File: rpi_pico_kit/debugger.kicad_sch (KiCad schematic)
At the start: 34 parts, among them J3 USB_B_Mini, U2 RP2040, U3 NCP1117-3.3_SOT223, U4 W25Q128JVS, Y1 12MHz

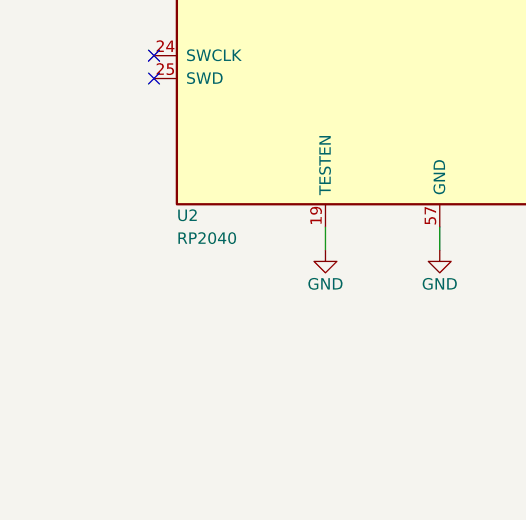
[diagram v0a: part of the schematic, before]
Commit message: changed transistors to unused gates of 7414
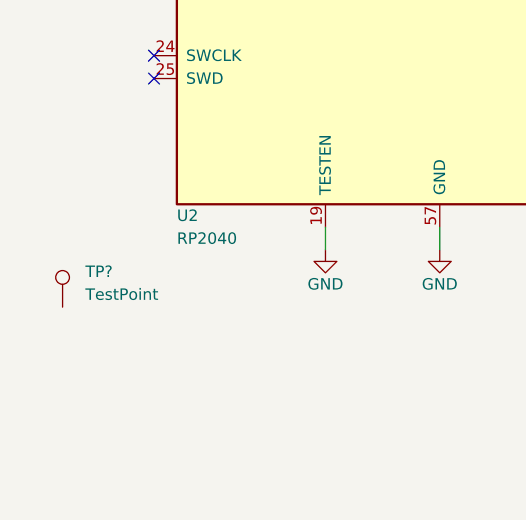
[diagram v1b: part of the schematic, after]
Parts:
- added TP?: TestPoint, symbol Connector:TestPoint
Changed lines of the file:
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@@
     (effects (font (size 1.27 1.27)) (justify left))
+  )
+  (symbol (lib_id "Connector:TestPoint") (at 27.94 168.91 0) (unit 1)
+    (in_bom yes) (on_board yes) (fields_autoplaced)
+    (property "Reference" "TP?" (id 0) (at 30.48 164.973 0)
+      (effects (font (size 1.27 1.27)) (justify left))
+    )
+    (property "Value" "TestPoint" (id 1) (at 30.48 167.513 0)
+      (effects (font (size 1.27 1.27)) (justify left))
+    )
+    (property "Footprint" "" (id 2) (at 33.02 168.91 0)
+      (effects (font (size 1.27 1.27)) hide)
+    )
+    (property "Datasheet" "~" (id 3) (at 33.02 168.91 0)
+      (effects (font (size 1.27 1.27)) hide)
+    )
+    (pin "1")
   )
   (symbol (lib_id "MCU_RaspberryPi_RP2040:RP2040") (at 69.85 109.22 0) (unit 1)

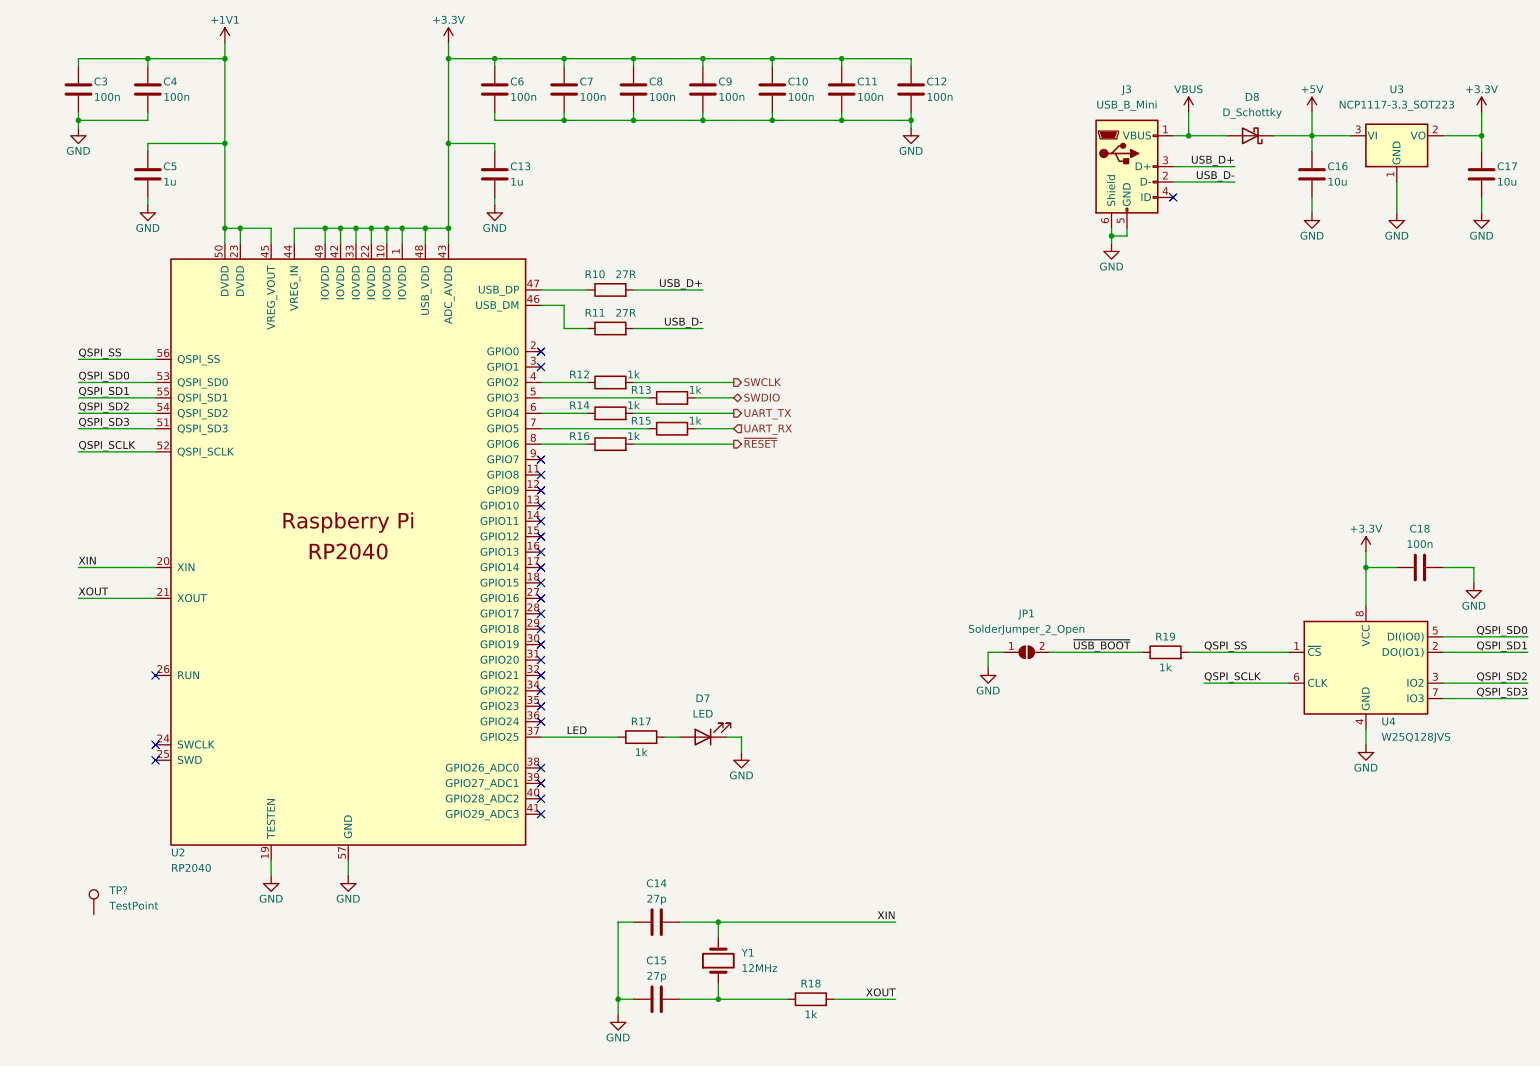
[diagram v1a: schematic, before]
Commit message: added test pads for uart and swd of debugger
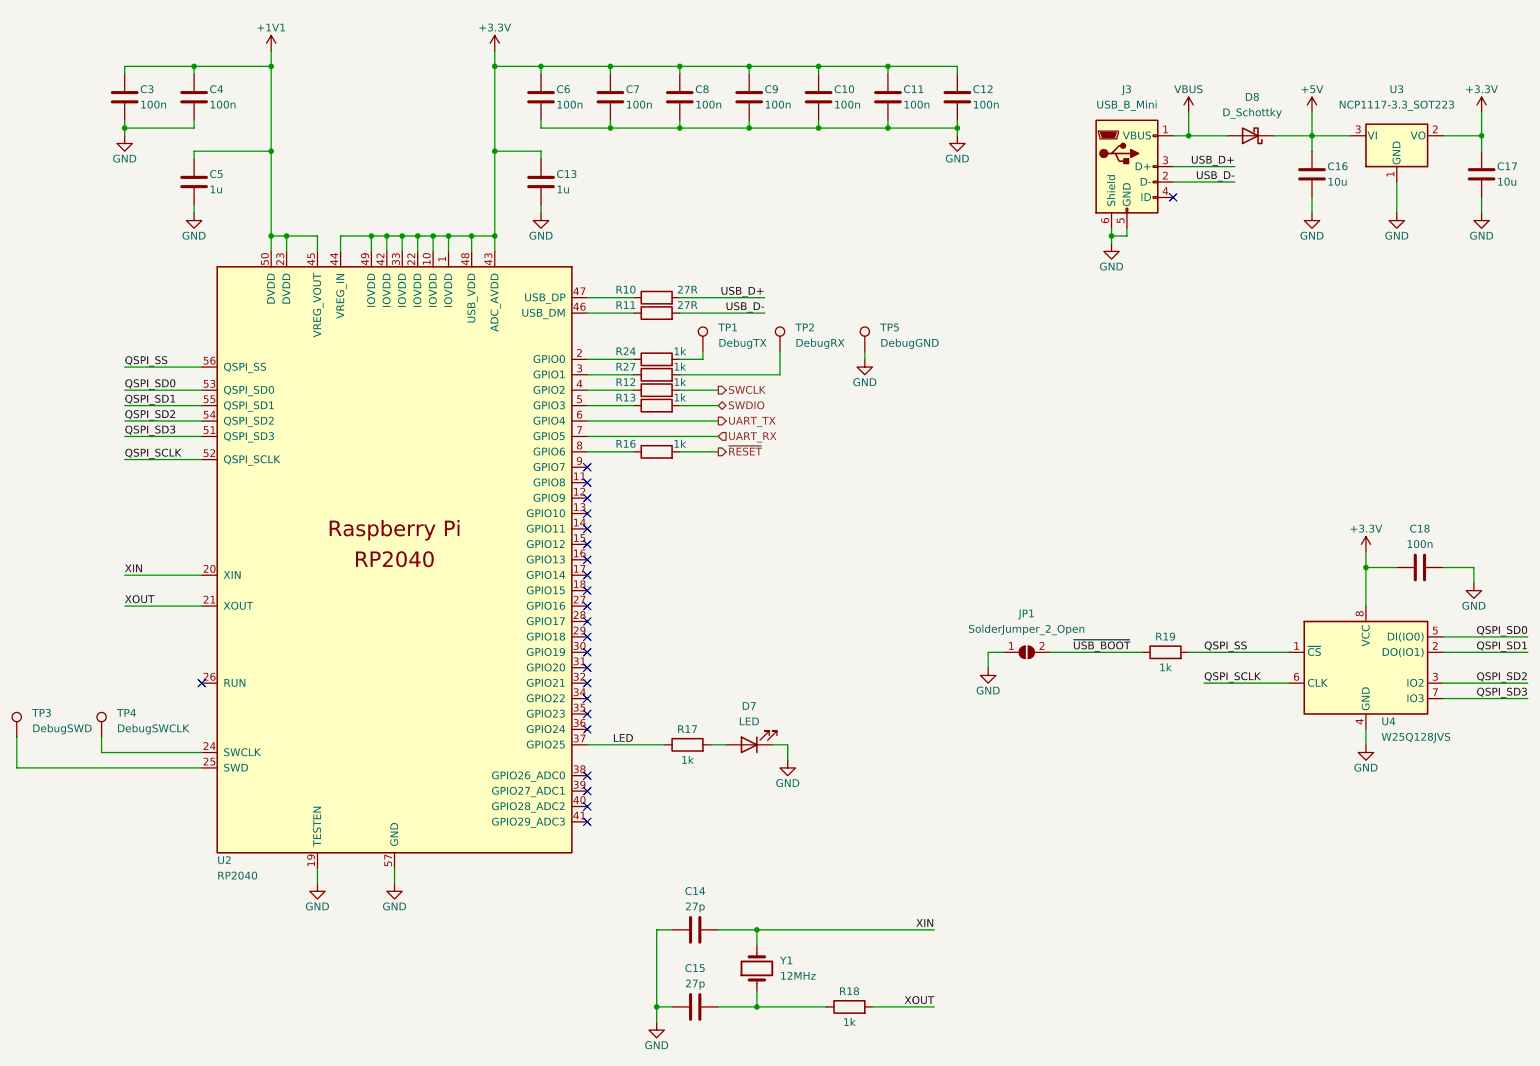
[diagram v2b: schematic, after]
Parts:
- removed R14, R15: 1k, Resistor_SMD:R_0805_2012Metric_Pad1.20x1.40mm_HandSolder, symbol Device:R
- added R24, R27: 1k, Resistor_SMD:R_0805_2012Metric_Pad1.20x1.40mm_HandSolder, symbol Device:R
- added TP2: DebugRX, TestPoint:TestPoint_Pad_D1.0mm, symbol Connector:TestPoint
- added TP3: DebugSWD, TestPoint:TestPoint_Pad_D1.0mm, symbol Connector:TestPoint
- added TP4: DebugSWCLK, TestPoint:TestPoint_Pad_D1.0mm, symbol Connector:TestPoint
- added TP5: DebugGND, TestPoint:TestPoint_Pad_D1.0mm, symbol Connector:TestPoint
- TP1: renamed from TP?; value TestPoint -> DebugTX; footprint (none) -> TestPoint:TestPoint_Pad_D1.5mm
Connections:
- net GND: now also TP5.1
- net UART_RX: now also U2.7 (GPIO5)
- net UART_TX: now also U2.6 (GPIO4)
- net at TP1.1: now also R24.2
- net at U2.2 (GPIO0): now also R24.1
- net at U2.24 (SWCLK): now also TP4.1
- net at U2.25 (SWD): now also TP3.1
- net at U2.3 (GPIO1): now also R27.1
- new net: R27.2, TP2.1
- no-connect marks 28 -> 24
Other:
- moved on the sheet: C10, C11, C12, C13, C14, C15, C3, C4, C5, C6, C7, C8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

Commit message: added some footprints
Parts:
- C16, C17: footprint (none) -> Capacitor_SMD:C_0805_2012Metric_Pad1.18x1.45mm_HandSolder
- D7: footprint LED_SMD:LED_1206_3216Metric_Pad1.42x1.75mm_HandSolder -> LED_SMD:LED_0805_2012Metric_Pad1.15x1.40mm_HandSolder
- JP1: footprint TestPoint:TestPoint_2Pads_Pitch2.54mm_Drill0.8mm -> (none)
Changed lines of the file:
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@@
       (effects (font (size 1.27 1.27)))
     )
-    (property "Footprint" "TestPoint:TestPoint_2Pads_Pitch2.54mm_Drill0.8mm" (id 2) (at 181.61 125.73 0)
+    (property "Footprint" "" (id 2) (at 181.61 125.73 0)
       (effects (font (size 1.27 1.27)) hide)
     )
@@
       (effects (font (size 1.27 1.27)) (justify right))
     )
-    (property "Footprint" "" (id 2) (at 227.6348 43.18 0)
+    (property "Footprint" "Capacitor_SMD:C_0805_2012Metric_Pad1.18x1.45mm_HandSolder" (id 2) (at 227.6348 43.18 0)
       (effects (font (size 1.27 1.27)) hide)
     )
@@
       (effects (font (size 1.27 1.27)))
     )
-    (property "Footprint" "LED_SMD:LED_1206_3216Metric_Pad1.42x1.75mm_HandSolder" (id 2) (at 135.89 140.97 0)
+    (property "Footprint" "LED_SMD:LED_0805_2012Metric_Pad1.15x1.40mm_HandSolder" (id 2) (at 135.89 140.97 0)
       (effects (font (size 1.27 1.27)) hide)
     )
@@
       (effects (font (size 1.27 1.27)) (justify right))
     )
-    (property "Footprint" "" (id 2) (at 255.5748 43.18 0)
-      (effects (font (size 1.27 1.27)) hide)
-    )
+    (property "Footprint" "Capacitor_SMD:C_0805_2012Metric_Pad1.18x1.45mm_HandSolder" (id 2) (at 255.5748 43.18 0)
+      (effects (font (size 1.27 1.27)) hide)
+    )

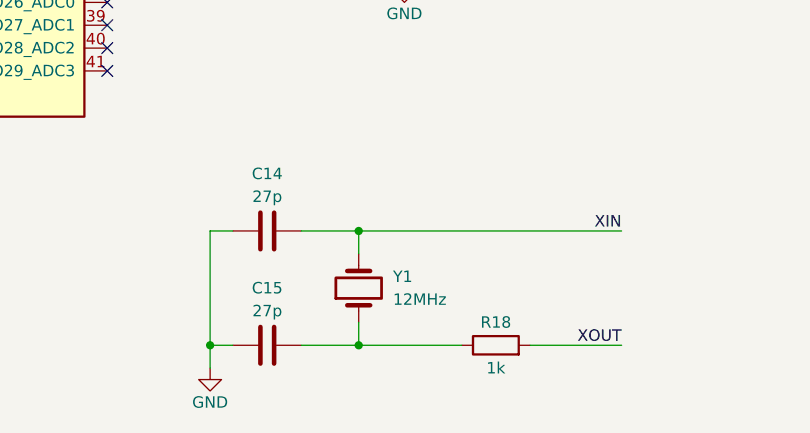
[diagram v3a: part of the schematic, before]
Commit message: added some MPNs, added fiducials
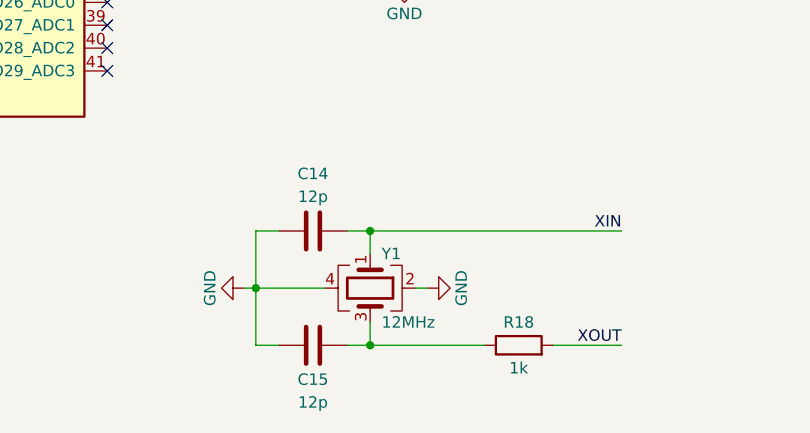
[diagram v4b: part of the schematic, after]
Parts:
- removed Y1: 12MHz, symbol Device:Crystal
- added Y1: 12MHz, Crystal:Crystal_SMD_Abracon_ABM3B-4Pin_5.0x3.2mm, symbol Device:Crystal_GND24
- C14, C15: value 27p -> 12p
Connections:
- net GND: now also Y1.2, Y1.4
- net XIN: now also Y1.1
- net at C15.2, R18.1: now also Y1.3
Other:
- moved on the sheet: C14, C15, R18

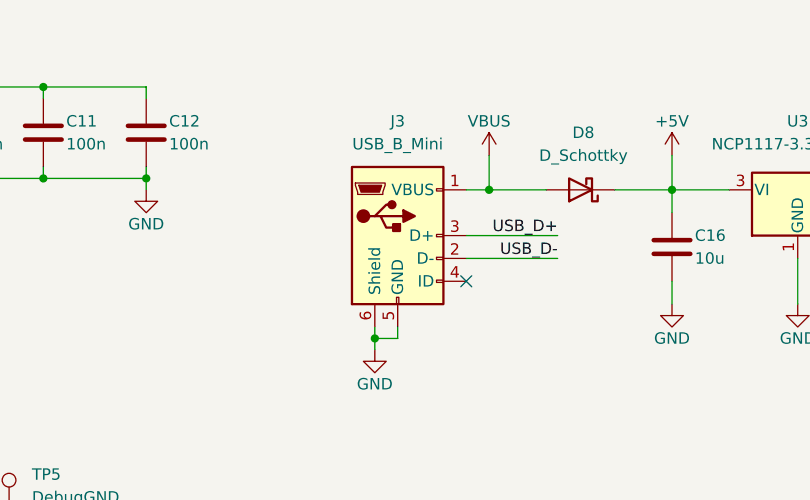
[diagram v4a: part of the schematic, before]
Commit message: edited 5V I2C, added some footprints, MPNs, added HDMI footprint library
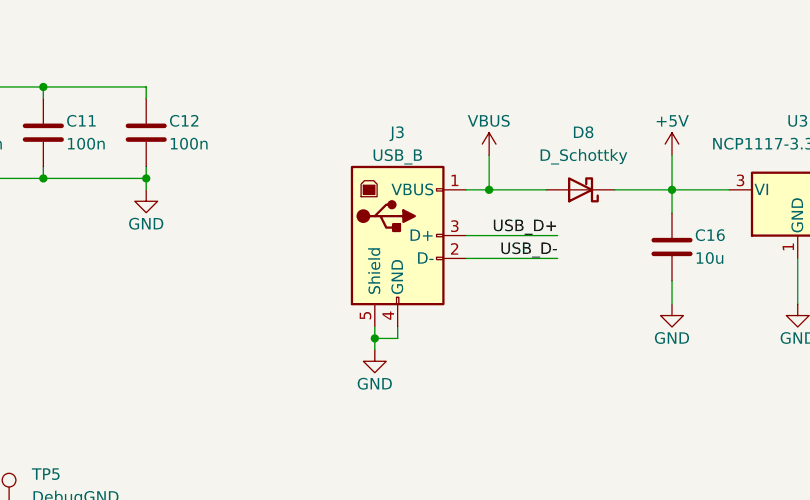
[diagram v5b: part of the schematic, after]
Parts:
- removed J3: USB_B_Mini, symbol RP2040_minimal:USB_B_Mini
- added J3: USB_B, Connector_USB:USB_B_Lumberg_2411_02_Horizontal, symbol Connector:USB_B
- D8: footprint (none) -> Diode_SMD:D_SMB; Manufacturer Part Number (none) -> STPS1L30U; Supplier (none) -> Digikey; Supplier Part URL (none) -> https://www.digikey.cz/en/products/detail/stmicroelectronic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
- JP1: footprint (none) -> Jumper:SolderJumper-2_P1.3mm_Open_RoundedPad1.0x1.5mm
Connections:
- net GND: now also J3.4 (GND), J3.5 (Shield)
- net USB_D+: now also J3.3 (D+)
- net USB_D-: now also J3.2 (D-)
- net VBUS: now also J3.1 (VBUS)
- no-connect marks 24 -> 23
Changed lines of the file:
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@@
   (junction (at 83.82 57.15) (diameter 0) (color 0 0 0 0)
   )
-  (no_connect (at 205.74 50.8))
   (no_connect (at 109.22 105.41))
   (no_connect (at 109.22 102.87))
@@
     (pin "2")
   )
+  (symbol (lib_id "Connector:USB_B") (at 198.12 45.72 0) (unit 1)
+    (in_bom yes) (on_board yes) (fields_autoplaced)
+    (property "Reference" "J3" (id 0) (at 198.12 34.29 0)
+      (effects (font (size 1.27 1.27)))
+    )
+    (property "Value" "USB_B" (id 1) (at 198.12 36.83 0)
+      (effects (font (size 1.27 1.27)))
+    )
+    (property "Footprint" "Connector_USB:USB_B_Lumberg_2411_02_Horizontal" (id 2) (at 201.93 46.99 0)
+      (effects (font (size 1.27 1.27)) hide)
+    )
+    (property "Datasheet" " ~" (id 3) (at 201.93 46.99 0)
+      (effects (font (size 1.27 1.27)) hide)
+    )
+    (property "Manufacturer Part Number" "USB-B1HSW6" (id 4) (at 198.12 45.72 0)
+      (effects (font (size 1.27 1.27)) hide)
+    )
+    (property "Supplier" "Digikey" (id 5) (at 198.12 45.72 0)
+      (effects (font (size 1.27 1.27)) hide)
+    )
+    (property "Supplier Part URL" "https://www.digikey.cz/en/products/detail/on-shore-technology-inc/USB-B1HSW6/2677743" (id 6) (at 198.12 45.72 0)
+      (effects (font (size 1.27 1.27)) hide)
+    )
+    (pin "1")
+    (pin "2")
+    (pin "3")
+    (pin "4")
+    (pin "5")
+  )
   (symbol (lib_id "Connector:TestPoint") (at 29.21 139.7 0) (unit 1)
     (in_bom yes) (on_board yes) (fields_autoplaced)
@@
       (effects (font (size 1.27 1.27)))
     )
-    (property "Footprint" "" (id 2) (at 218.44 40.64 0)
+    (property "Footprint" "Diode_SMD:D_SMB" (id 2) (at 218.44 40.64 0)
       (effects (font (size 1.27 1.27)) hide)
     )
     (property "Datasheet" "~" (id 3) (at 218.44 40.64 0)
+      (effects (font (size 1.27 1.27)) hide)
+    )
+    (property "Manufacturer Part Number" "STPS1L30U" (id 4) (at 218.44 40.64 0)
+      (effects (font (size 1.27 1.27)) hide)
+    )
+    (property "Supplier" "Digikey" (id 5) (at 218.44 40.64 0)
+      (effects (font (size 1.27 1.27)) hide)
+    )
+    (property "Supplier Part URL" "https://www.digikey.cz/en/products/detail/stmicroelectronics/STPS1L30U/603493" (id 6) (at 218.44 40.64 0)
       (effects (font (size 1.27 1.27)) hide)
     )
@@
       (effects (font (size 1.27 1.27)))
     )
-    (property "Footprint" "" (id 2) (at 181.61 125.73 0)
+    (property "Footprint" "Jumper:SolderJumper-2_P1.3mm_Open_RoundedPad1.0x1.5mm" (id 2) (at 181.61 125.73 0)
       (effects (font (size 1.27 1.27)) hide)
     )
@@
     (pin "2")
   )
-  (symbol (lib_id "RP2040_minimal:USB_B_Mini") (at 198.12 45.72 0) (unit 1)
-    (in_bom yes) (on_board yes) (fields_autoplaced)
-    (property "Reference" "J3" (id 0) (at 198.12 33.02 0)
-      (effects (font (size 1.27 1.27)))
-    )
-    (property "Value" "USB_B_Mini" (id 1) (at 198.12 35.56 0)
-      (effects (font (size 1.27 1.27)))
-    )
-    (property "Footprint" "" (id 2) (at 201.93 46.99 0)
-      (effects (font (size 1.27 1.27)) hide)
-    )
-    (property "Datasheet" "" (id 3) (at 201.93 46.99 0)
-      (effects (font (size 1.27 1.27)) hide)
-    )
-    (pin "1")
-    (pin "2")
-    (pin "3")
-    (pin "4")
-    (pin "5")
-    (pin "6")
-  )
   (symbol (lib_id "power:VBUS") (at 208.28 36.83 0) (unit 1)
